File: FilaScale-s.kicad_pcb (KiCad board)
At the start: 2 copper layers, 65 x 50 mm, 16 parts, among them J1 HX711MOD, J2 RFID, J3 EXP1, J4 Arduino_Nano_v3.x, J5 BME-280, J6 I2C 1, J7 I2C 2, M3 MountingHole_3.2mm_M3_ISO7380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

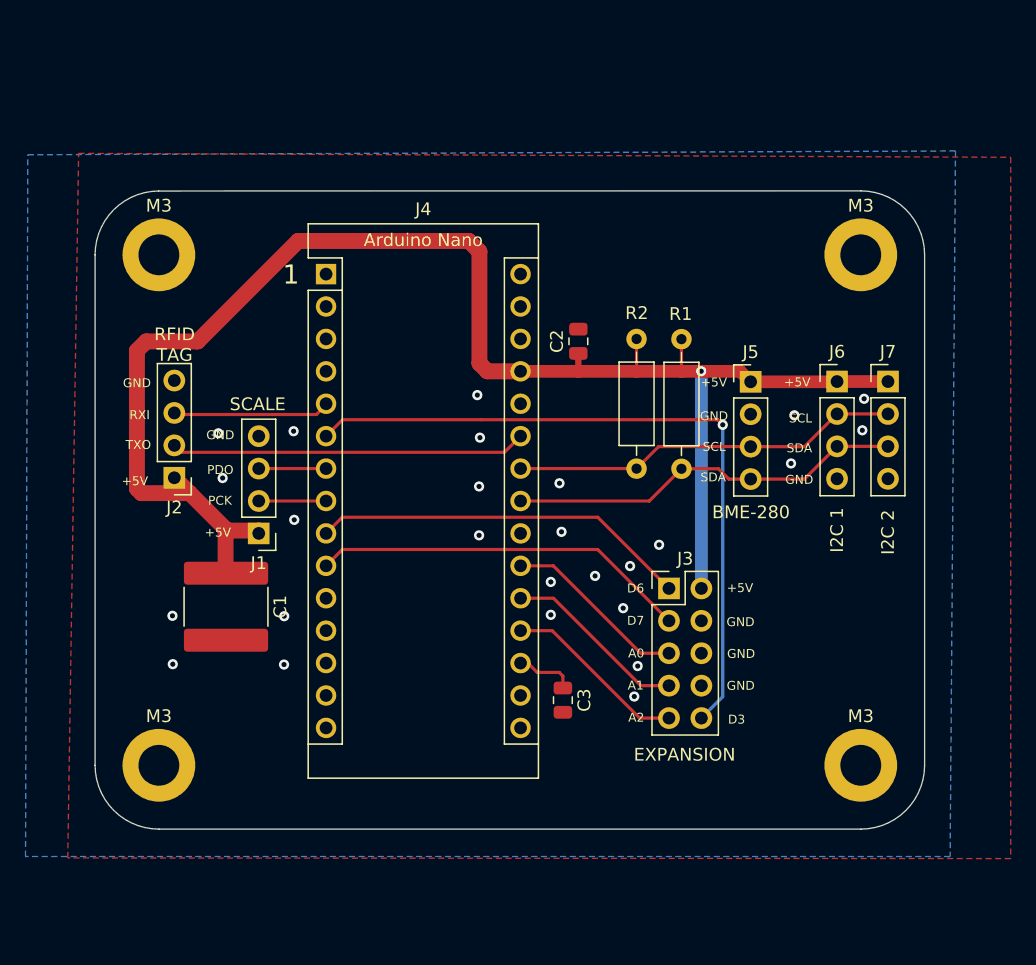
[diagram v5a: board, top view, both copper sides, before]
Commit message: Change layout to accommodate horizontal connectors, to miminize height
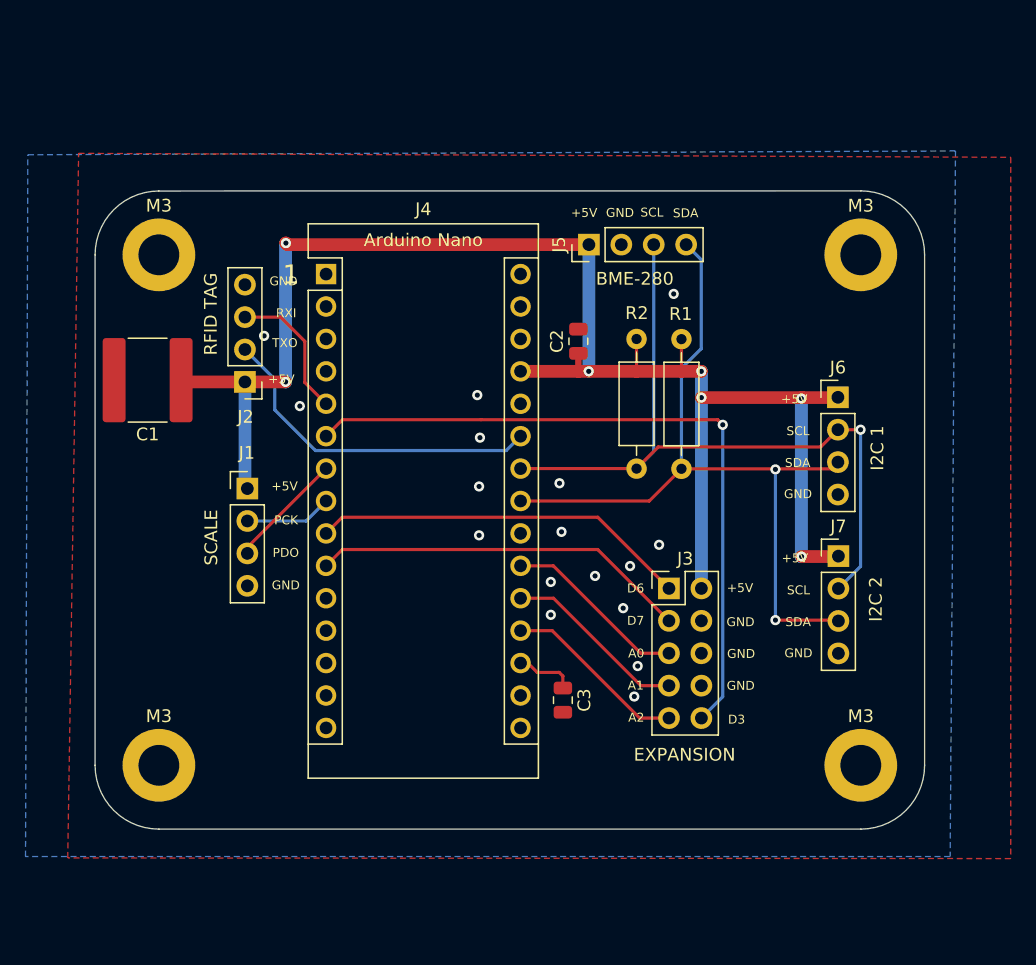
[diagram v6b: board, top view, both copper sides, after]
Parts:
- moved C1 18.8 mm to (42.1, 137.8), turned to 180 degrees
- moved J5 16.6 mm to (76.7, 127.2), turned to 90 degrees
- moved J7 14.2 mm to (96.2, 151.6)
- moved J2 9.33 mm to (49.7, 138.0)
- moved J1 3.62 mm to (49.9, 146.3), turned to 0 degrees
- moved J6 1.24 mm to (96.2, 139.2)
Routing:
- net /SDA: track 31.2 -> 61.7 mm, vias 0 -> 2
- net /SCL: track 30.6 -> 59.2 mm, vias 0 -> 1
- net /PD_DOUT: track 5.27 -> 9.20 mm
- net +5V: track 122.7 -> 125.1 mm, vias 1 -> 7
- net /PD_SCK: track 5.27 -> 6.82 mm
- net /RFID_RXI: track 12.4 -> 11.1 mm
- net /RFID_TXO: track 27.8 -> 26.7 mm
- net GND: vias 26 -> 17
